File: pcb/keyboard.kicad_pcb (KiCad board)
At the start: 2 copper layers, 216.8 x 97 mm, 50 parts, among them J1 TRRS, SW11 11, SW12 12, SW13 13, SW14 14, SW15 15, SW16 16, SW17 17, SW18 18, SW19 19, SW21 21, SW22 22, SW23 23, SW24 24, SW25 25, SW26 26, SW27 27, SW28 28, SW29 29, SW31 31, SW32 32, SW33 33, SW34 34, SW35 35, SW36 36, SW37 37, SW38 38, SW39 39, SW41 41, SW42 42, SW43 43, SW45 45, SW46 46, SW47 47, SW48 48, SW49 49, U1 EliteC

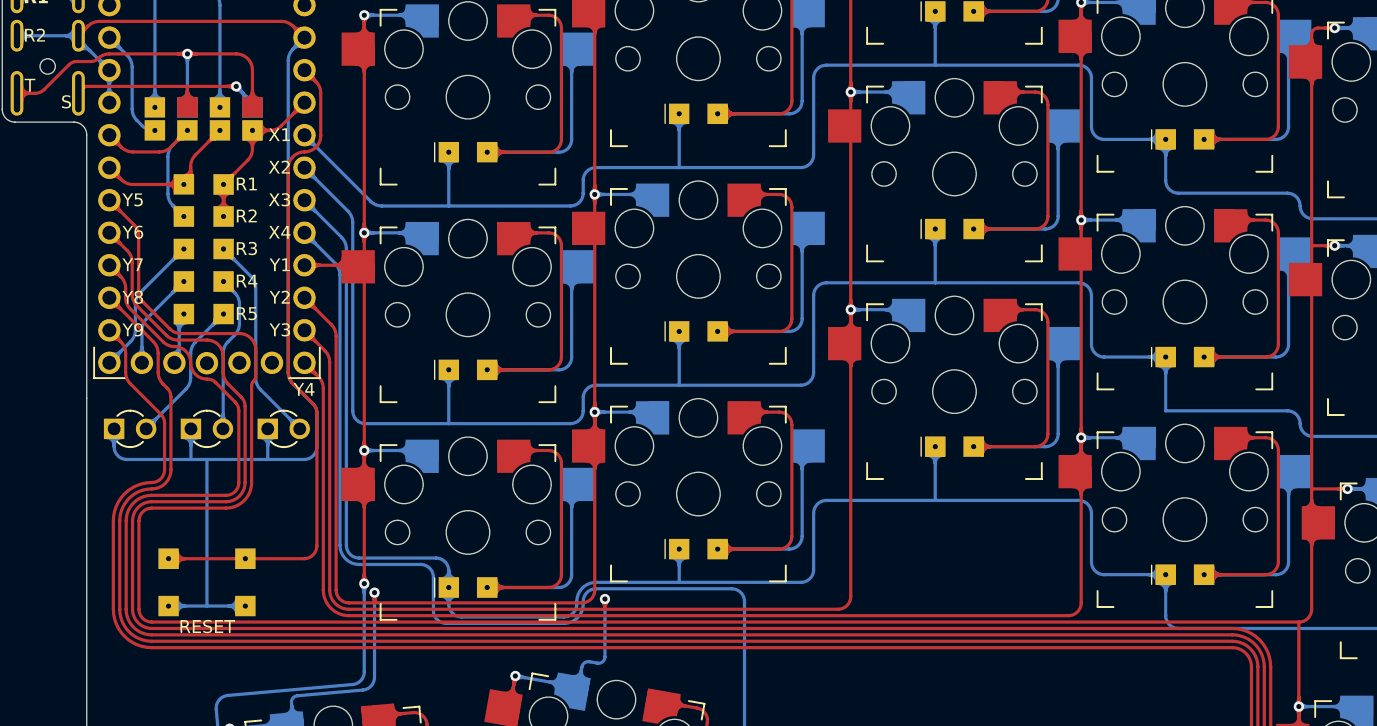
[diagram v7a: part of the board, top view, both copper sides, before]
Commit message: move col7 trace around controller
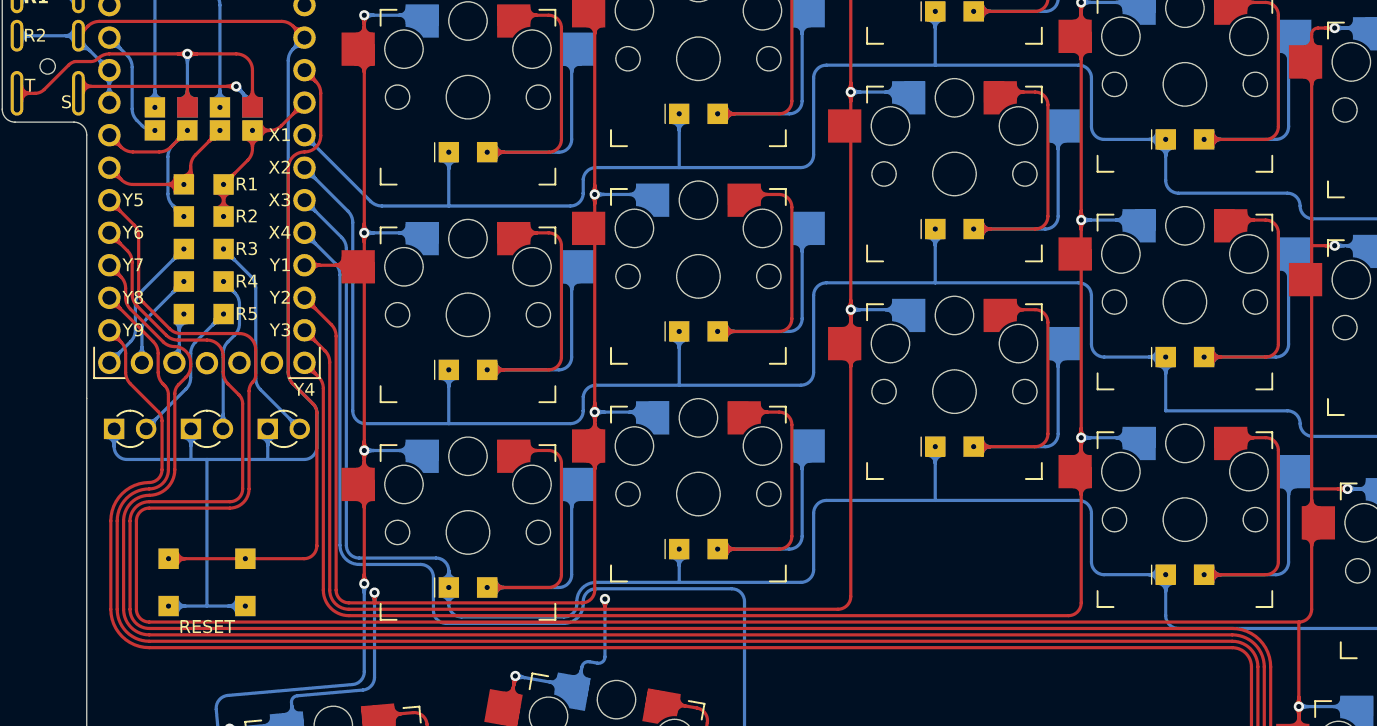
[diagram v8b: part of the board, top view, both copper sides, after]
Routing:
- net COL7: track 330.1 -> 323.6 mm
- net Net-(J1-Pad4): track 21.8 -> 24.0 mm
